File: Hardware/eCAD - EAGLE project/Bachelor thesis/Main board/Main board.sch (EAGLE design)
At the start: 110 parts, among them IC1 ESP32-WROOM-32E_M113EH3200PH3Q, IC10 SMS3.3.TCT, IC2 BC660K-GL, IC3 SMS3.3.TCT, IC4 AP9101CK6-ADTRG1, IC5 FDS6898A, IC6 MCP73871-2CCI_ML, IC7 ME6211C33M5G-N, IC8 ME6211C33M5G-N, IC9 SMS3.3.TCT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

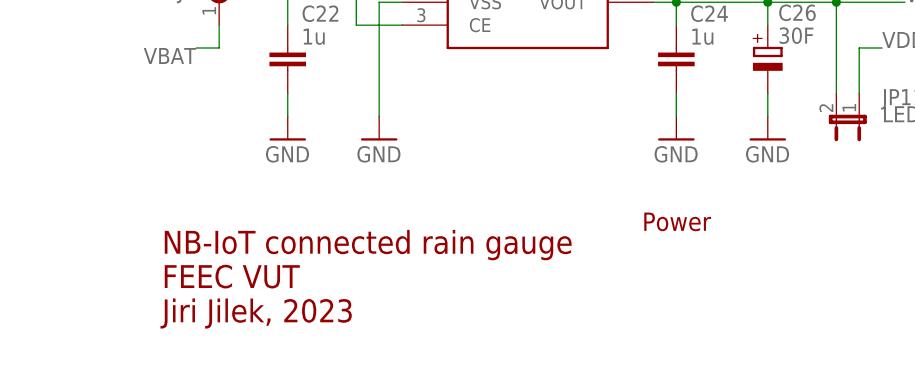
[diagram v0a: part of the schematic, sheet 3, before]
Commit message: Reorder of files, added 3D models and NodeRED flow
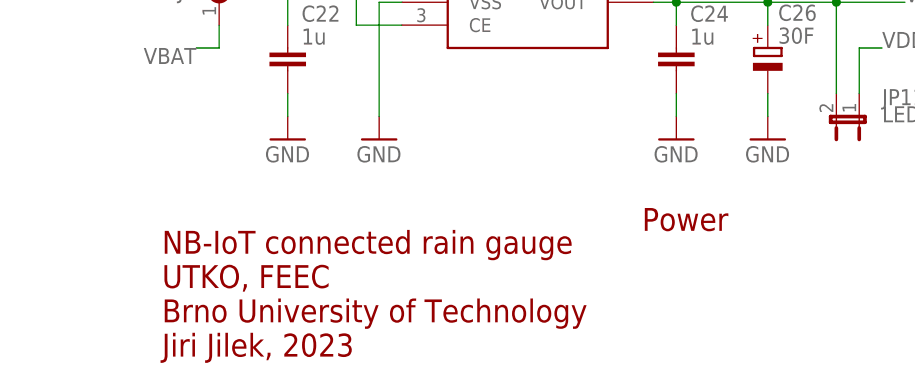
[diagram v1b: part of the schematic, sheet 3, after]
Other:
- note added: "NB-IoT connected rain gauge UTKO, FEEC Brno University of Technology Jiri Jilek, 2023"
- note removed: "NB-IoT connected rain gauge FEEC VUT Jiri Jilek, 2023"
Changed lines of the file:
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@@
 <text x="217.17" y="20.32" size="2.54" layer="94">ESP32</text>
 <text x="163.83" y="20.32" size="2.54" layer="94" align="top-left">NB-IoT connected rain gauge
-FEEC VUT
+UTKO, FEEC
+Brno University of Technology
 Jiri Jilek, 2023</text>
 </plain>
@@
 <text x="101.6" y="43.18" size="1.778" layer="97">VIO_SEL grounded for 3.3V logic levels</text>
 <text x="163.83" y="20.32" size="2.54" layer="94" align="top-left">NB-IoT connected rain gauge
-FEEC VUT
+UTKO, FEEC
+Brno University of Technology
 Jiri Jilek, 2023</text>
 </plain>
@@
 <sheet>
 <plain>
-<text x="217.17" y="20.32" size="2.032" layer="94">Power</text>
+<text x="217.17" y="20.32" size="2.54" layer="94">Power</text>
 <text x="165.1" y="154.94" size="1.778" layer="97">VPCC: 1.23=(R15/R15+R16)*VPCC
 With 100k and 330k R we get VPCC voltage 5.29 V.
@@
 <text x="172.72" y="157.48" size="1.778" layer="97"></text>
 <text x="163.83" y="20.32" size="2.54" layer="94" align="top-left">NB-IoT connected rain gauge
-FEEC VUT
+UTKO, FEEC
+Brno University of Technology
 Jiri Jilek, 2023</text>
 </plain>
@@
 <text x="104.14" y="22.86" size="1.778" layer="97">I2C addr: 0x76</text>
 <text x="163.83" y="20.32" size="2.54" layer="94" align="top-left">NB-IoT connected rain gauge
-FEEC VUT
+UTKO, FEEC
+Brno University of Technology
 Jiri Jilek, 2023</text>
 </plain>
